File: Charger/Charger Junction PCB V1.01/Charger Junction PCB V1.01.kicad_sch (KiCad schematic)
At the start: 9 parts, among them J2 Tractive Battery, J3 Charger, J4 J1772 Plug, J7 E-Stop, SW1 J1772 Dummy Enable (BMS Overr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

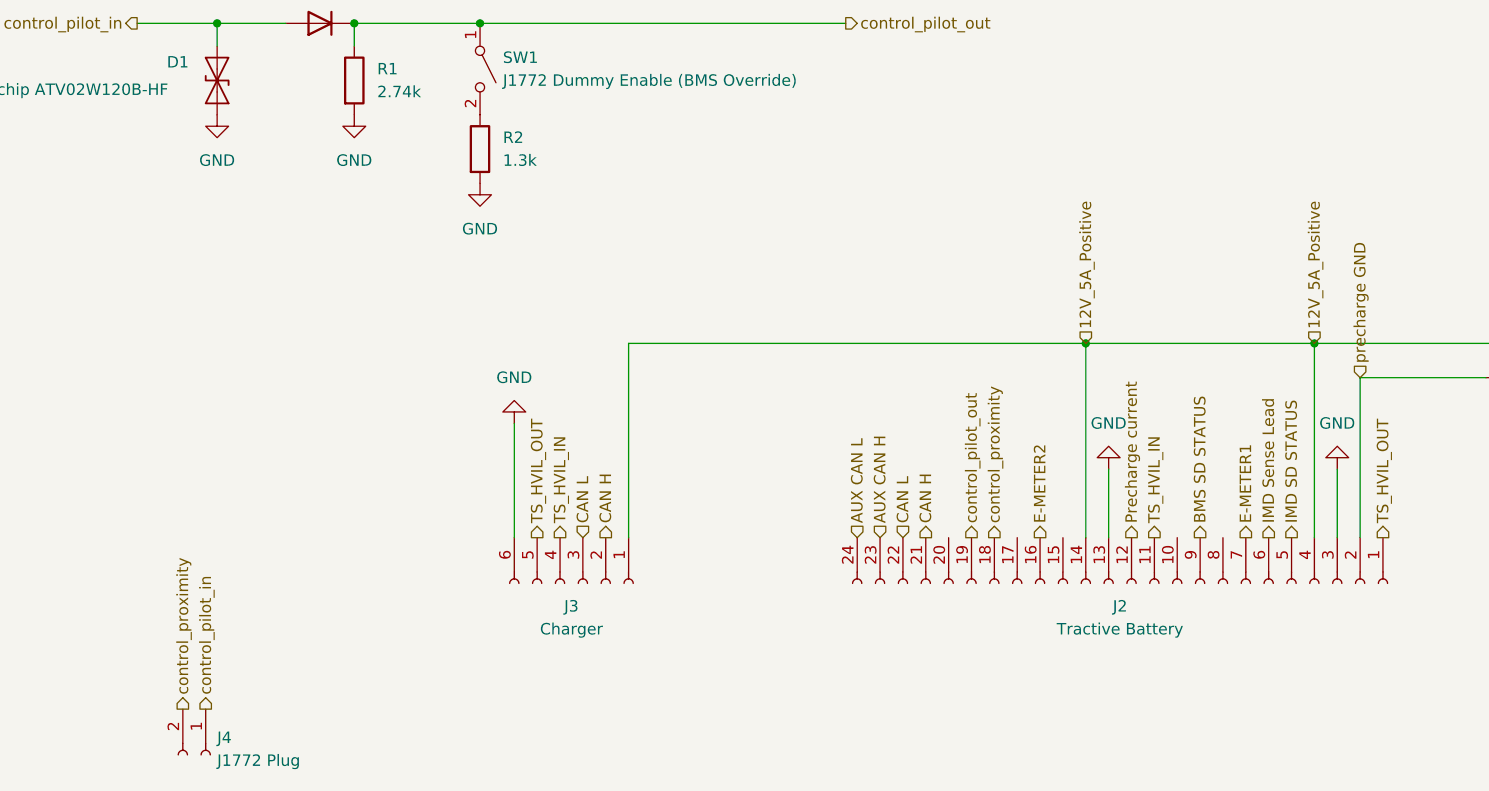
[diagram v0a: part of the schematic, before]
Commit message: Added switch connector
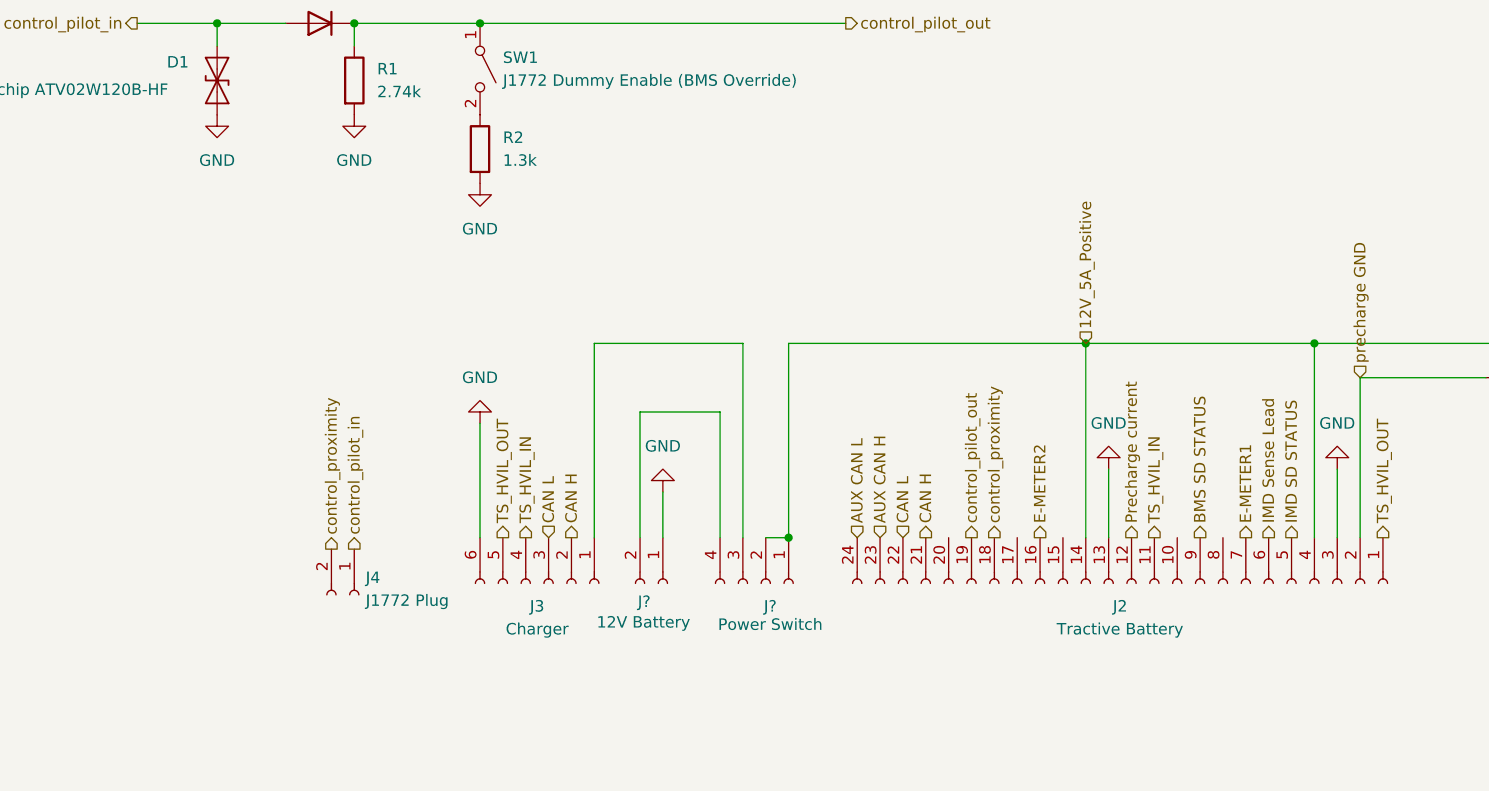
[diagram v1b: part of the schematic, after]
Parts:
- added J?: 12V Battery, symbol Connector:Conn_01x02_Socket
- added J?: Power Switch, symbol Connector:Conn_01x04_Socket
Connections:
- net 12V_5A_Positive: now also J?.1 (Pin_1), J?.2 (Pin_2); no longer J3.1 (Pin_1)
- net GND: now also J?.1 (Pin_1)
- new net: J?.2 (Pin_2), J?.4 (Pin_4)
- new net: J3.1 (Pin_1), J?.3 (Pin_3)
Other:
- moved on the sheet: J3, J4

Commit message: Added schottky diode
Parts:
- added D?: Nexperia PMEG045V100EPE-QZ, Diode_SMD:D_SMC, symbol Diode:B360
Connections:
- net at J?.3 (Pin_3): now also D?.1 (K); no longer J3.1 (Pin_1)
- new net: D?.2 (A), J3.1 (Pin_1)
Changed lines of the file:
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@@
-	(wire
-		(pts
-			(xy 140.97 120.65) (xy 157.48 120.65)
-		)
-		(stroke
-			(width 0)
-			(type default)
-		)
-	)
 	(wire
 		(pts
@@
 	(wire
 		(pts
+			(xy 140.97 120.65) (xy 146.05 120.65)
+		)
+		(stroke
+			(width 0)
+			(type default)
+		)
+	)
+	(wire
+		(pts
 			(xy 220.98 120.65) (xy 259.08 120.65)
 		)
@@
 		(pts
 			(xy 140.97 142.24) (xy 140.97 120.65)
+		)
+		(stroke
+			(width 0)
+			(type default)
+		)
+	)
+	(wire
+		(pts
+			(xy 153.67 120.65) (xy 157.48 120.65)
 		)
 		(stroke
@@
 					(unit 1)
 				)
+			)
+		)
+	)
+	(symbol
+		(lib_id "Diode:B360")
+		(at 149.86 120.65 180)
+		(unit 1)
+		(body_style 1)
+		(exclude_from_sim no)
+		(in_bom yes)
+		(on_board yes)
+		(in_pos_files yes)
+		(dnp no)
+		(fields_autoplaced yes)
+		(property "Reference" "D?"
+			(at 150.1775 114.3 0)
+			(show_name no)
+			(do_not_autoplace no)
+			(effects
+				(font
+					(size 1.27 1.27)
+				)
+			)
+		)
+		(property "Value" "Nexperia PMEG045V100EPE-QZ"
+			(at 150.1775 116.84 0)
+			(show_name no)
+			(do_not_autoplace no)
+			(effects
+				(font
+					(size 1.27 1.27)
+				)
+			)
+		)
+		(property "Footprint" "Diode_SMD:D_SMC"
+			(at 149.86 116.205 0)
+			(hide yes)
+			(show_name no)
+			(do_not_autoplace no)
+			(effects
+				(font
+					(size 1.27 1.27)
+				)
+			)
+		)
+		(property "Datasheet" "http://www.jameco.com/Jameco/Products/ProdDS/1538777.pdf"
+			(at 149.86 120.65 0)
+			(hide yes)
+			(show_name no)
+			(do_not_autoplace no)
+			(effects
+				(font
+					(size 1.27 1.27)
+				)
+			)
+		)
+		(property "Description" "60V 3A Schottky Barrier Rectifier Diode, SMC"
+			(at 149.86 120.65 0)
+			(hide yes)
+			(show_name no)
+			(do_not_autoplace no)
+			(effects
+				(font
+					(size 1.27 1.27)
+				)
+			)
+		)
+		(pin "2"
+		)
+		(pin "1"
+		)
+		(instances
+			(project "Charger Junction PCB V1.01"
+				(path "/75f6fa4d-fba8-4d29-9299-863888d8bb95"
+					(reference "D?")
+					(unit 1)
+				)

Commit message: 12 Pin Update
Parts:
- removed J2: Tractive Battery, symbol Connector:Conn_01x24_Socket
- added J1: Tractive Battery, symbol Connector:Conn_01x12_Pin
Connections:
- net 12V_5A_Positive: now also J1.4 (Pin_4), J1.8 (Pin_8)
- net CAN H: now also J1.11 (Pin_11)
- net CAN L: now also J1.12 (Pin_12)
- net GND: now also J1.2 (Pin_2), J1.3 (Pin_3), J1.7 (Pin_7)
- net Precharge current: now also J1.6 (Pin_6)
- net TS_HVIL_IN: now also J1.5 (Pin_5)
- net TS_HVIL_OUT: now also J1.1 (Pin_1)
- net control_pilot_out: now also J1.10 (Pin_10)
- net control_proximity: now also J1.9 (Pin_9)

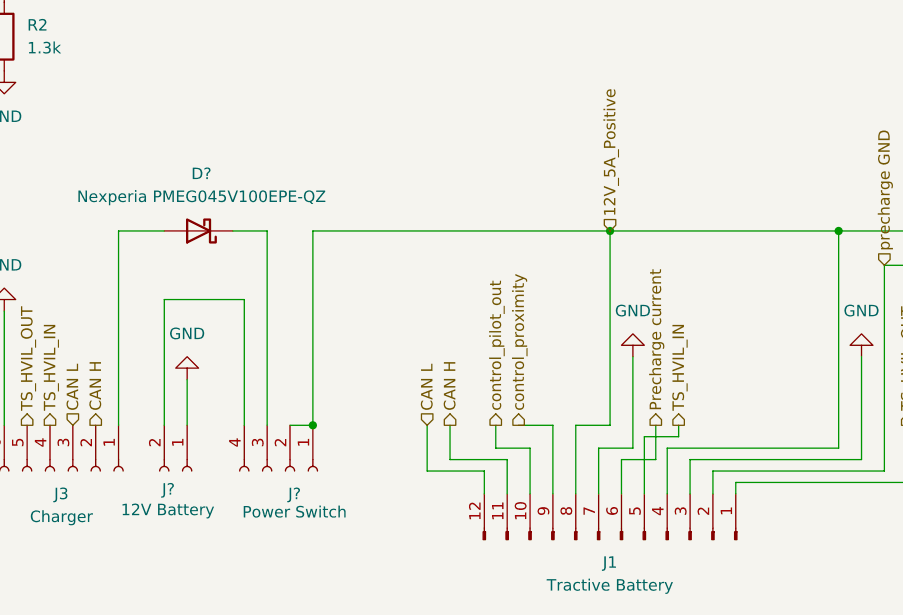
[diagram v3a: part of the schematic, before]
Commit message: Began working on assigning footprints
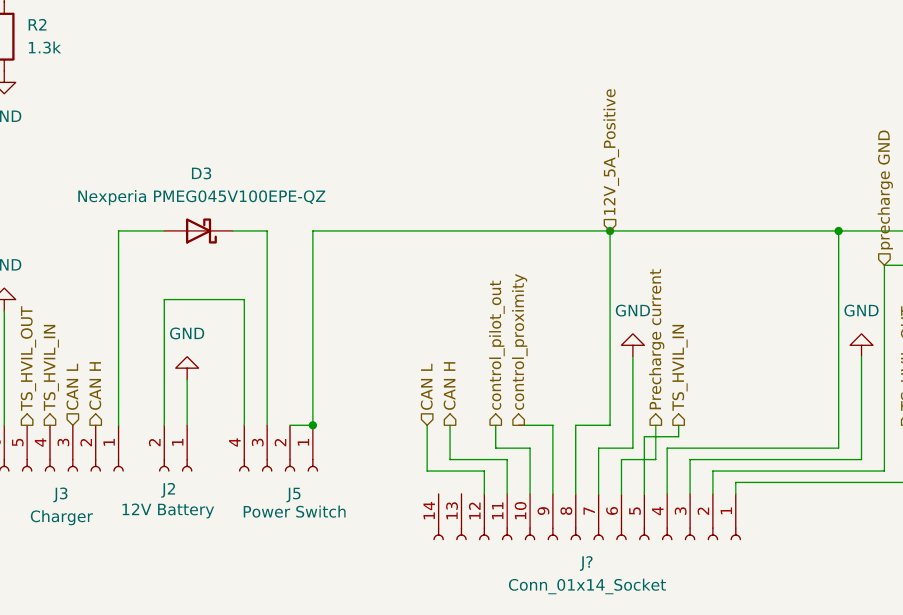
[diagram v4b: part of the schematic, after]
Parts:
- removed J1: Tractive Battery, symbol Connector:Conn_01x12_Pin
- added J?: Conn_01x14_Socket, symbol Connector:Conn_01x14_Socket
- D1: footprint Diode_SMD:D_SMA -> Diode_SMD:D_SOD-123F
- D2: footprint Diode_SMD:D_SOD-123 -> (none)
- D3: renamed from D?; footprint Diode_SMD:D_SMC -> (none)
- J3, J4: footprint Package_DFN_QFN:QFN-20-1EP_5x5mm_P0.65mm_EP3.35x3.35mm -> (none)
- gave numbers to parts that had none: 2
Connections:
- net 12V_5A_Positive: now also J?.4 (Pin_4), J?.8 (Pin_8)
- net CAN H: now also J?.11 (Pin_11)
- net CAN L: now also J?.12 (Pin_12)
- net GND: now also J?.2 (Pin_2), J?.3 (Pin_3), J?.7 (Pin_7)
- net Precharge current: now also J?.6 (Pin_6)
- net TS_HVIL_IN: now also J?.5 (Pin_5)
- net TS_HVIL_OUT: now also J?.1 (Pin_1)
- net control_pilot_out: now also J?.10 (Pin_10)
- net control_proximity: now also J?.9 (Pin_9)
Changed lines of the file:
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@@
-	)
-	(symbol
-		(lib_id "Connector:Conn_01x12_Pin")
-		(at 196.85 154.94 270)
-		(mirror x)
-		(unit 1)
-		(body_style 1)
-		(exclude_from_sim no)
-		(in_bom yes)
-		(on_board yes)
-		(in_pos_files yes)
-		(dnp no)
-		(property "Reference" "J1"
-			(at 195.58 157.48 90)
-			(show_name no)
-			(do_not_autoplace no)
-			(effects
-				(font
-					(size 1.27 1.27)
-				)
-			)
-		)
-		(property "Value" "Tractive Battery"
-			(at 195.58 160.02 90)
-			(show_name no)
-			(do_not_autoplace no)
-			(effects
-				(font
-					(size 1.27 1.27)
-				)
-			)
-		)
-		(property "Footprint" ""
-			(at 196.85 154.94 0)
-			(hide yes)
-			(show_name no)
-			(do_not_autoplace no)
-			(effects
-				(font
-					(size 1.27 1.27)
-				)
-			)
-		)
-		(property "Datasheet" ""
-			(at 196.85 154.94 0)
-			(hide yes)
-			(show_name no)
-			(do_not_autoplace no)
-			(effects
-				(font
-					(size 1.27 1.27)
-				)
-			)
-		)
-		(property "Description" "Generic connector, single row, 01x12, script generated"
-			(at 196.85 154.94 0)
-			(hide yes)
-			(show_name no)
-			(do_not_autoplace no)
-			(effects
-				(font
-					(size 1.27 1.27)
-				)
-			)
-		)
-		(pin "6"
-		)
-		(pin "1"
-		)
-		(pin "4"
-		)
-		(pin "2"
-		)
-		(pin "3"
-		)
-		(pin "11"
-		)
-		(pin "10"
-		)
-		(pin "8"
-		)
-		(pin "9"
-		)
-		(pin "5"
-		)
-		(pin "12"
-		)
-		(pin "7"
-		)
-		(instances
-			(project "Charger Junction PCB V1.01"
-				(path "/75f6fa4d-fba8-4d29-9299-863888d8bb95"
-					(reference "J1")
-					(unit 1)
-				)
-			)
-		)
 	)
 	(symbol
@@
 		(in_pos_files yes)
 		(dnp no)
-		(property "Reference" "J?"
+		(property "Reference" "J2"
 			(at 145.796 149.352 90)
 			(show_name no)
@@
 			(project "Charger Junction PCB V1.01"
 				(path "/75f6fa4d-fba8-4d29-9299-863888d8bb95"
-					(reference "J?")
+					(reference "J2")
 					(unit 1)
 				)
@@
 		(dnp no)
 		(fields_autoplaced yes)
-		(property "Reference" "D?"
+		(property "Reference" "D3"
 			(at 150.1775 114.3 0)
 			(show_name no)
@@
 			)
 		)
-		(property "Footprint" "Diode_SMD:D_SMC"
+		(property "Footprint" ""
 			(at 149.86 116.205 0)
 			(hide yes)
@@
 			(project "Charger Junction PCB V1.01"
 				(path "/75f6fa4d-fba8-4d29-9299-863888d8bb95"
-					(reference "D?")
+					(reference "D3")
 					(unit 1)
 				)
@@
 			)
 		)
-		(property "Footprint" "Package_DFN_QFN:QFN-20-1EP_5x5mm_P0.65mm_EP3.35x3.35mm"
+		(property "Footprint" ""
 			(at 114.3 148.59 0)
 			(hide yes)
@@
 			)
 		)
-		(property "Footprint" "Package_DFN_QFN:QFN-20-1EP_5x5mm_P0.65mm_EP3.35x3.35mm"
+		(property "Footprint" ""
 			(at 135.89 147.32 0)
 			(hide yes)
@@
 		(in_pos_files yes)
 		(dnp no)
-		(property "Reference" "J?"
+		(property "Reference" "J5"
 			(at 160.528 149.86 90)
 			(show_name no)
@@
 		)
 		(pin "2"
+		)
+		(instances
+			(project "Charger Junction PCB V1.01"
+				(path "/75f6fa4d-fba8-4d29-9299-863888d8bb95"
+					(reference "J5")
+					(unit 1)
+				)
+			)
+		)
+	)
+	(symbol
+		(lib_id "Connector:Conn_01x14_Socket")
+		(at 194.31 154.94 270)
+		(unit 1)
+		(body_style 1)
+		(exclude_from_sim no)
+		(in_bom yes)
+		(on_board yes)
+		(in_pos_files yes)
+		(dnp no)
+		(fields_autoplaced yes)
+		(property "Reference" "J?"
+			(at 193.04 157.48 90)
+			(show_name no)
+			(do_not_autoplace no)
+			(effects
+				(font
+					(size 1.27 1.27)
+				)
+			)
+		)
+		(property "Value" "Conn_01x14_Socket"
+			(at 193.04 160.02 90)
+			(show_name no)
+			(do_not_autoplace no)
+			(effects
+				(font
+					(size 1.27 1.27)
+				)
+			)
+		)
+		(property "Footprint" ""
+			(at 194.31 154.94 0)
+			(hide yes)
+			(show_name no)
+			(do_not_autoplace no)
+			(effects
+				(font
+					(size 1.27 1.27)
+				)
+			)
+		)
+		(property "Datasheet" ""
+			(at 194.31 154.94 0)
+			(hide yes)
+			(show_name no)
+			(do_not_autoplace no)
+			(effects
+				(font
+					(size 1.27 1.27)
+				)
+			)
+		)
+		(property "Description" "Generic connector, single row, 01x14, script generated"
+			(at 194.31 154.94 0)
+			(hide yes)
+			(show_name no)
+			(do_not_autoplace no)
+			(effects
+				(font
+					(size 1.27 1.27)
+				)
+			)
+		)
+		(pin "13"
+		)
+		(pin "11"
+		)
+		(pin "14"
+		)
+		(pin "3"
+		)
+		(pin "10"
+		)
+		(pin "12"
+		)
+		(pin "9"
+		)
+		(pin "1"
+		)
+		(pin "4"
+		)
+		(pin "5"
+		)
+		(pin "6"
+		)
+		(pin "7"
+		)
+		(pin "2"
+		)
+		(pin "8"
 		)
 		(instances
@@
 			)
 		)
-		(property "Footprint" "Diode_SMD:D_SMA"
+		(property "Footprint" "Diode_SMD:D_SOD-123F"
 			(at 104.14 91.44 0)
 			(hide yes)
@@
 			)
 		)
-		(property "Footprint" "Diode_SMD:D_SOD-123"
+		(property "Footprint" ""
 			(at 110.49 85.09 0)
 			(hide yes)
